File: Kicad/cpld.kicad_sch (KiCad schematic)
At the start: 16 parts, among them J2 Conn_01x06_Pin, U7 AMS1117-3.3, U9 XC95144XL-TQ144

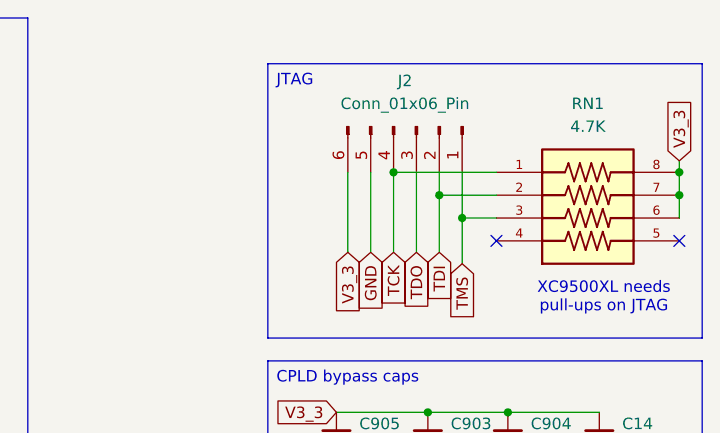
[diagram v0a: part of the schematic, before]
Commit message: Add more LCSC parts and mark some parts DNP
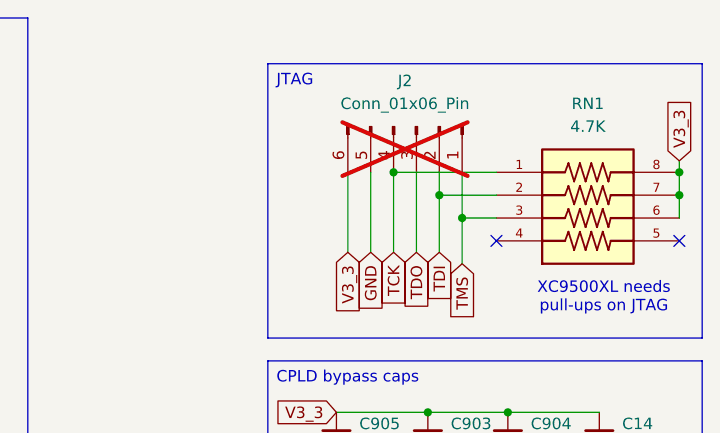
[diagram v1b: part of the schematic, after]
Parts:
- C14, C901, C902, C903, C904, C905, C906: LCSC Part # (none) -> C14663
- J2: LCSC Part # (none) -> C6332199; now not fitted
- RN1: footprint YC324-FK-071KL:RESCAXS127P508X320X70-8N -> CAY16_102J4LF:BO_CAY16; LCSC Part # (none) -> C327044
- U7: LCSC Part # (none) -> C6186
- U9: LCSC Part # (none) -> C1521137
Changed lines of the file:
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@@
 		(in_bom yes)
 		(on_board yes)
-		(dnp no)
+		(dnp yes)
 		(fields_autoplaced yes)
 		(property "Reference" "J2"
@@
 		(property "Description" "Generic connector, single row, 01x06, script generated"
 			(at 166.37 25.4 0)
+			(effects
+				(font
+					(size 1.27 1.27)
+				)
+				(hide yes)
+			)
+		)
+		(property "LCSC Part #" "C6332199"
+			(at 166.37 25.4 90)
 			(effects
 				(font
@@
 			)
 		)
+		(property "LCSC Part #" "C14663"
+			(at 157.48 68.58 0)
+			(effects
+				(font
+					(size 1.27 1.27)
+				)
+				(hide yes)
+			)
+		)
 		(pin "1"
 		)
@@
 			)
 		)
+		(property "LCSC Part #" "C1521137"
+			(at 67.31 104.14 0)
+			(effects
+				(font
+					(size 1.27 1.27)
+				)
+				(hide yes)
+			)
+		)
 		(pin "17"
 		)
@@
 			)
 		)
+		(property "LCSC Part #" ""
+			(at 160.02 97.79 0)
+			(effects
+				(font
+					(size 1.27 1.27)
+				)
+				(hide yes)
+			)
+		)
 		(pin "1"
 		)
@@
 			)
 		)
+		(property "LCSC Part #" "C14663"
+			(at 177.8 68.58 0)
+			(effects
+				(font
+					(size 1.27 1.27)
+				)
+				(hide yes)
+			)
+		)
 		(pin "1"
 		)
@@
 			)
 		)
+		(property "LCSC Part #" "C14663"
+			(at 176.53 59.69 0)
+			(effects
+				(font
+					(size 1.27 1.27)
+				)
+				(hide yes)
+			)
+		)
 		(pin "1"
 		)
@@
 		(property "Description" "Ferrite bead, small symbol"
 			(at 111.76 68.58 0)
+			(effects
+				(font
+					(size 1.27 1.27)
+				)
+				(hide yes)
+			)
+		)
+		(property "LCSC Part #" ""
+			(at 111.76 68.58 90)
 			(effects
 				(font
@@
 			)
 		)
+		(property "LCSC Part #" "C14663"
+			(at 157.48 59.69 0)
+			(effects
+				(font
+					(size 1.27 1.27)
+				)
+				(hide yes)
+			)
+		)
 		(pin "1"
 		)
@@
 			)
 		)
+		(property "LCSC Part #" "C14663"
+			(at 186.69 59.69 0)
+			(effects
+				(font
+					(size 1.27 1.27)
+				)
+				(hide yes)
+			)
+		)
 		(pin "2"
 		)
@@
 			)
 		)
+		(property "LCSC Part #" ""
+			(at 184.15 97.79 0)
+			(effects
+				(font
+					(size 1.27 1.27)
+				)
+				(hide yes)
+			)
+		)
 		(pin "1"
 		)
@@
 			)
 		)
+		(property "LCSC Part #" ""
+			(at 111.76 154.94 90)
+			(effects
+				(font
+					(size 1.27 1.27)
+				)
+				(hide yes)
+			)
+		)
 		(pin "1"
 		)
@@
 		(property "Description" "Ferrite bead, small symbol"
 			(at 111.76 144.78 0)
+			(effects
+				(font
+					(size 1.27 1.27)
+				)
+				(hide yes)
+			)
+		)
+		(property "LCSC Part #" ""
+			(at 111.76 144.78 90)
 			(effects
 				(font
@@
 			)
 		)
+		(property "LCSC Part #" "C14663"
+			(at 167.64 59.69 0)
+			(effects
+				(font
+					(size 1.27 1.27)
+				)
+				(hide yes)
+			)
+		)
 		(pin "2"
 		)
@@
 			)
 		)
+		(property "LCSC Part #" "C6186"
+			(at 173.99 92.71 0)
+			(effects
+				(font
+					(size 1.27 1.27)
+				)
+				(hide yes)
+			)
+		)
 		(pin "3"
 		)
@@
 			)
 		)
-		(property "Footprint" "YC324-FK-071KL:RESCAXS127P508X320X70-8N"
+		(property "Footprint" "CAY16_102J4LF:BO_CAY16"
 			(at 185.42 35.56 0)
 			(effects
@@
 				)
 				(justify bottom)
+				(hide yes)
+			)
+		)
+		(property "LCSC Part #" "C327044"
+			(at 185.42 35.56 0)
+			(effects
+				(font
+					(size 1.27 1.27)
+				)
 				(hide yes)
 			)
@@
 			(at 167.64 68.58 0)
 			(effects
+				(font
+					(size 1.27 1.27)
+				)
+				(hide yes)
+			)
+		)
+		(property "LCSC Part #" "C14663"
+			(at 167.64 68.58 0)
+			(effects

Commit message: Add remaining part numbers, remove C20, C30, C31
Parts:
- C701: LCSC Part # (none) -> C7194
- C702: LCSC Part # (none) -> C696813
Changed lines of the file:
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@@
 			)
 		)
-		(property "LCSC Part #" ""
+		(property "LCSC Part #" "C7194"
 			(at 160.02 97.79 0)
 			(effects
@@
 			)
 		)
-		(property "LCSC Part #" ""
+		(property "LCSC Part #" "C696813"
 			(at 184.15 97.79 0)
 			(effects

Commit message: Fix LCSC parts issues
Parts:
- FB6, FB7, FB8: LCSC Part # (none) -> C95177
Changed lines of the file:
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@@
 			)
 		)
-		(property "LCSC Part #" ""
+		(property "LCSC Part #" "C95177"
 			(at 111.76 68.58 90)
 			(effects
@@
 			)
 		)
-		(property "LCSC Part #" ""
+		(property "LCSC Part #" "C95177"
 			(at 111.76 154.94 90)
 			(effects
@@
 			)
 		)
-		(property "LCSC Part #" ""
+		(property "LCSC Part #" "C95177"
 			(at 111.76 144.78 90)
 			(effects

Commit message: Clean up schematics
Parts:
- removed C14: 100nF, Capacitor_SMD:C_0603_1608Metric_Pad1.08x0.95mm_HandSolder, symbol Device:C_Small
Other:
- moved on the sheet: C701, C702, C901, C902, C903, C904, C905, C906, U7

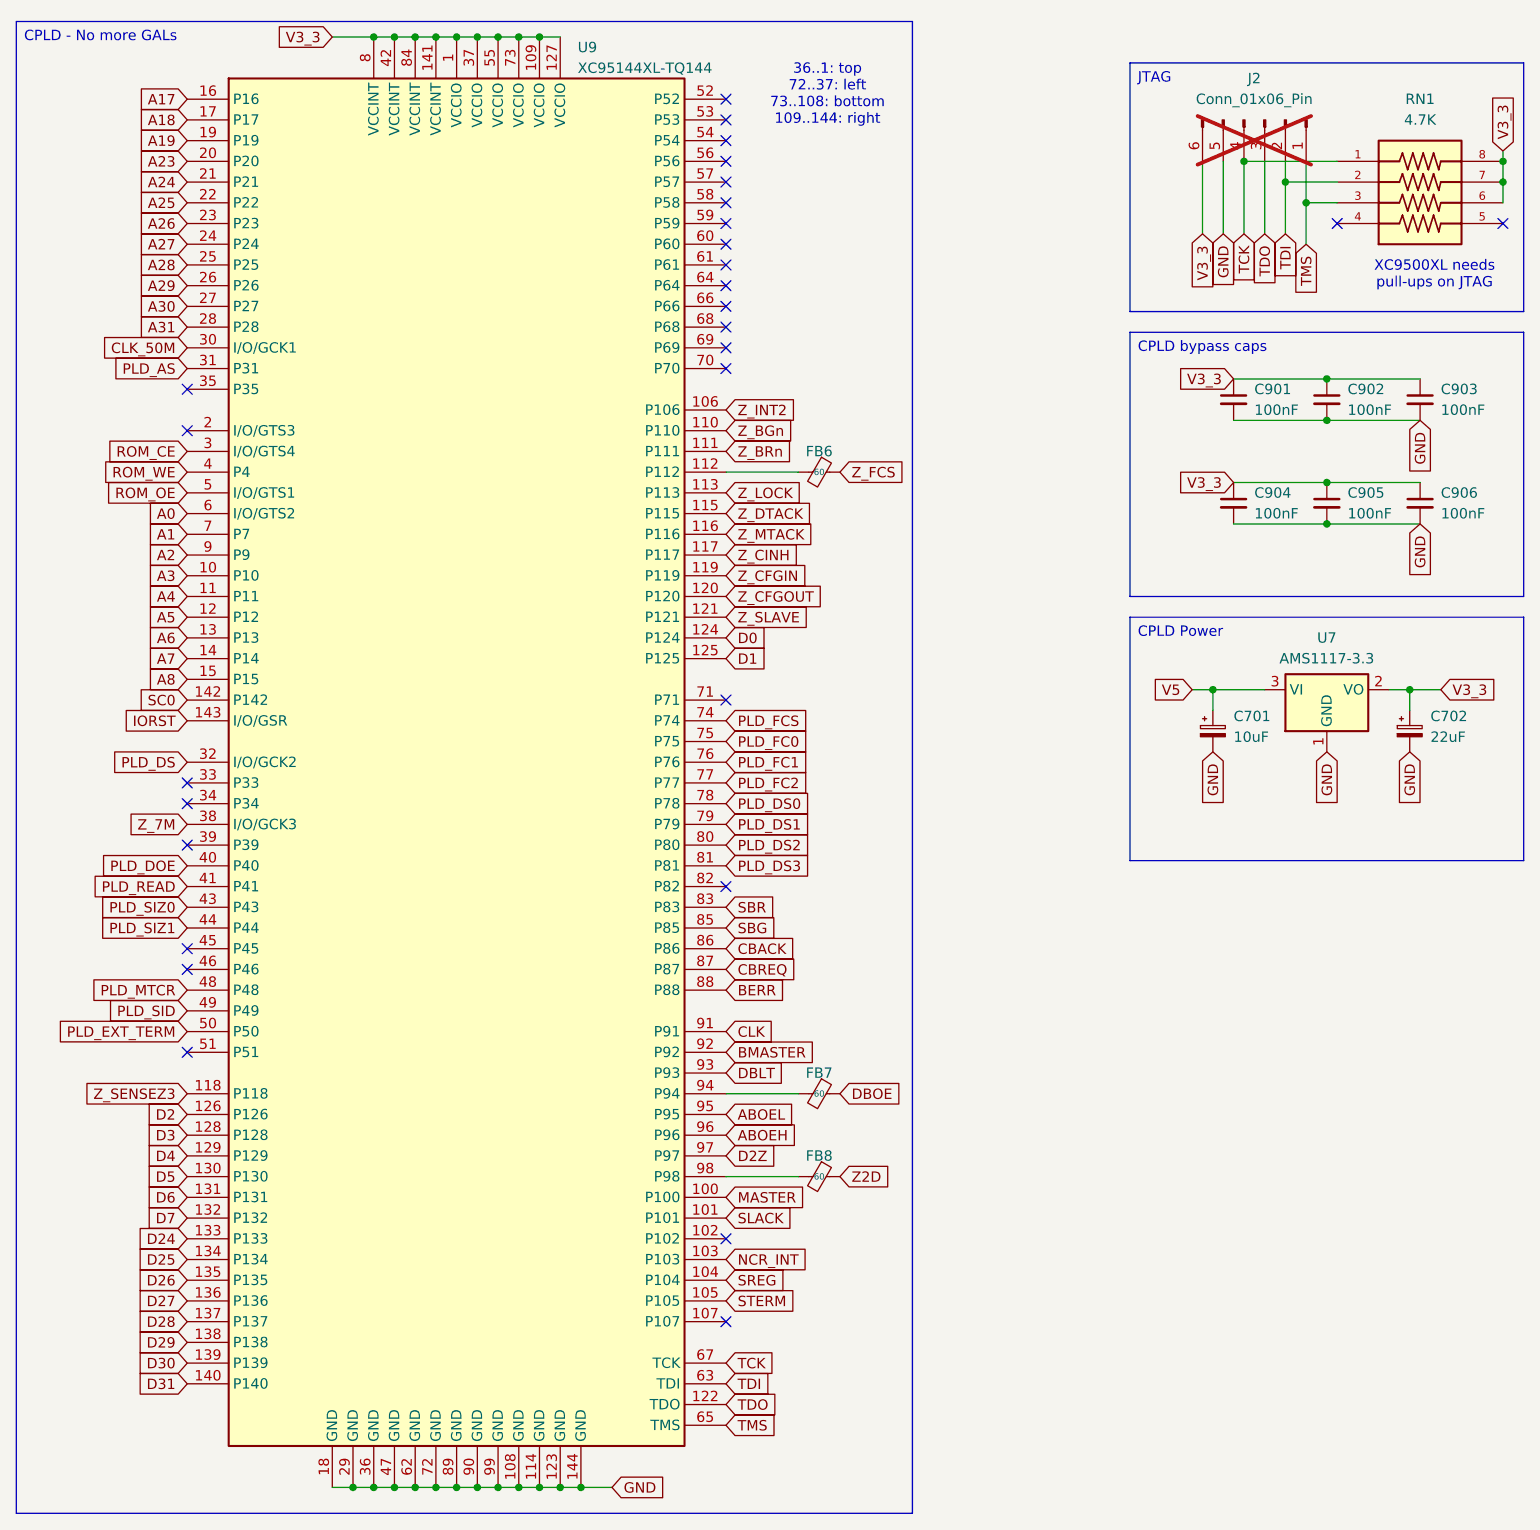
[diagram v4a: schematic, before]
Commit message: Add fiducials and clean up schematics
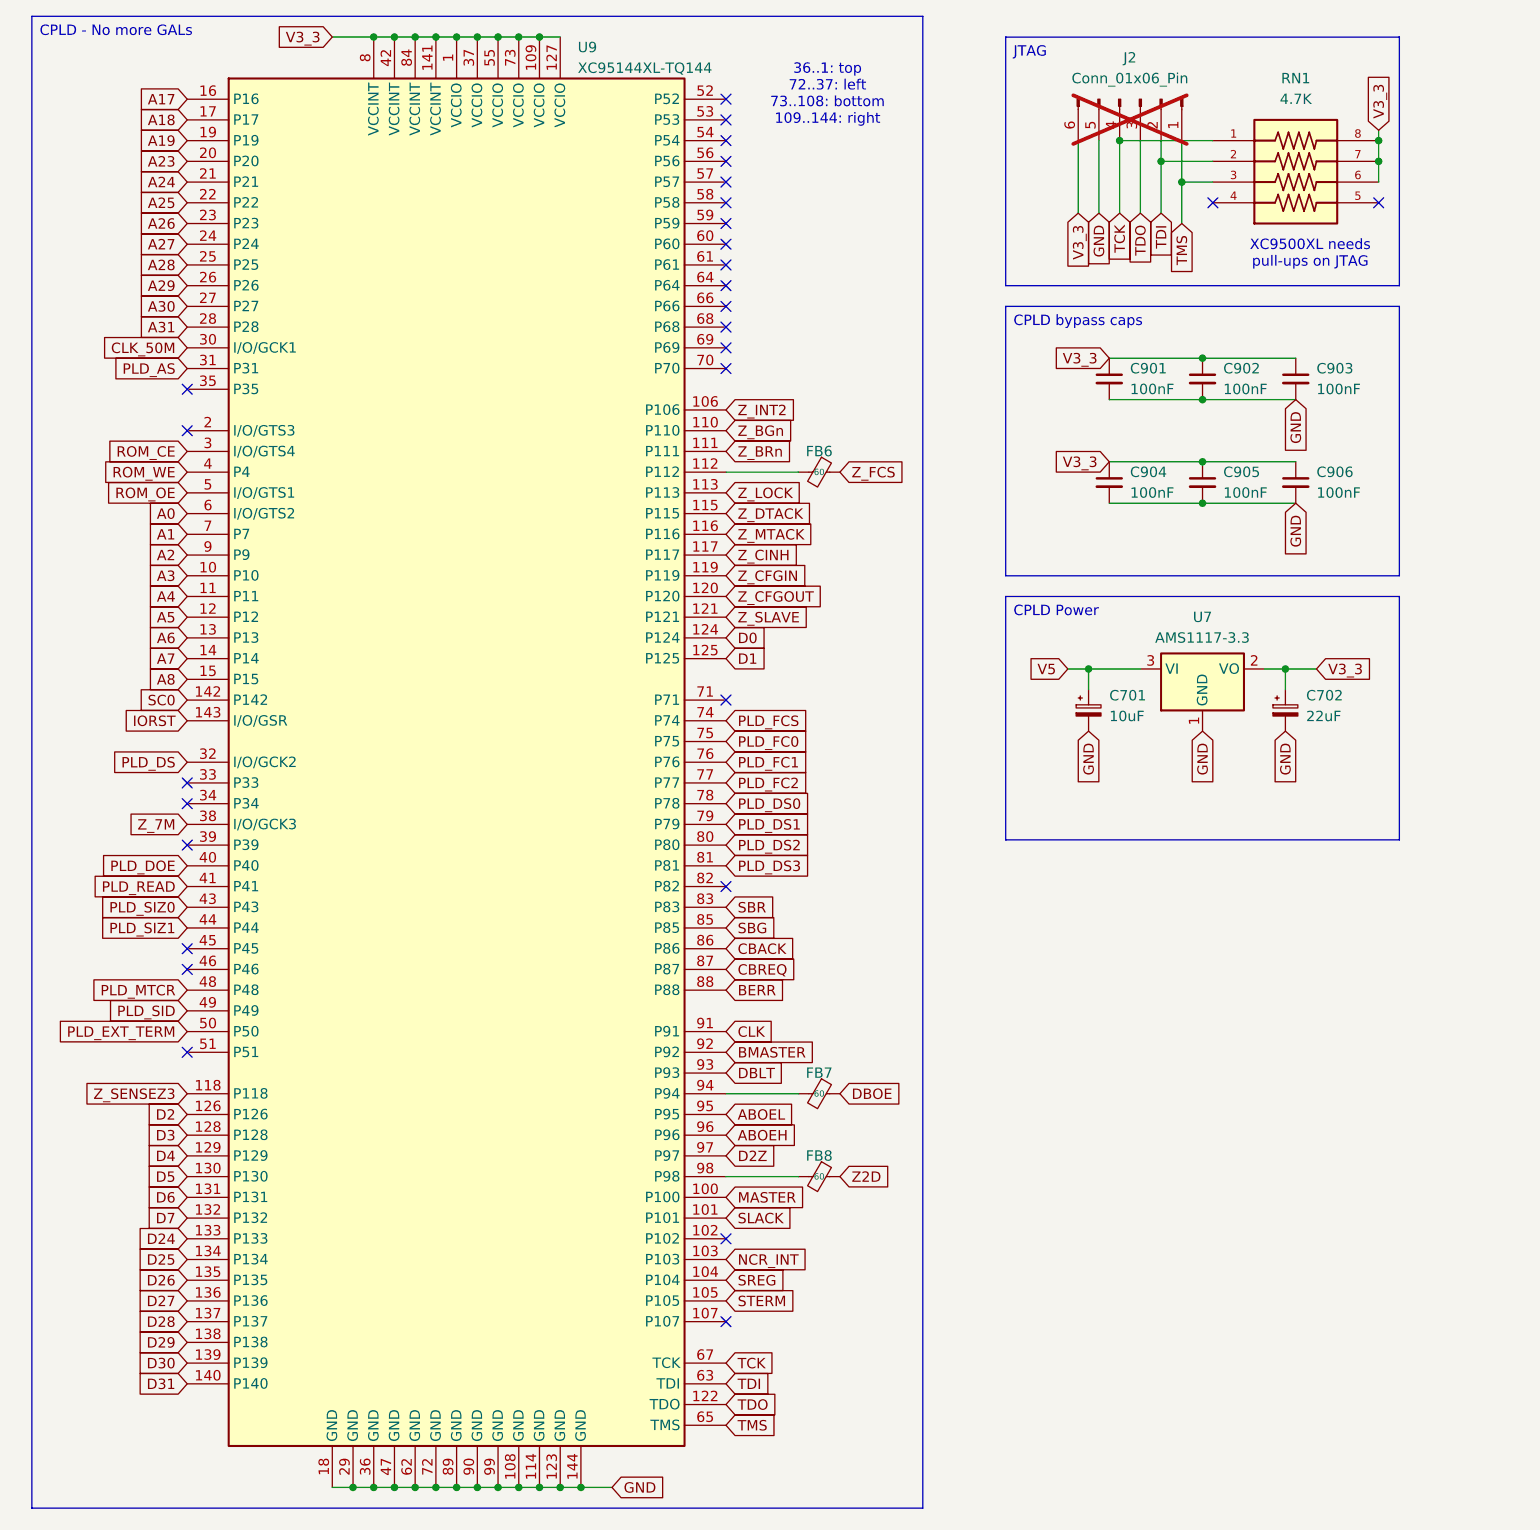
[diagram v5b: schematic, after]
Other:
- moved on the sheet: C701, C702, C901, C902, C903, C904, C905, C906, J2, RN1, U7

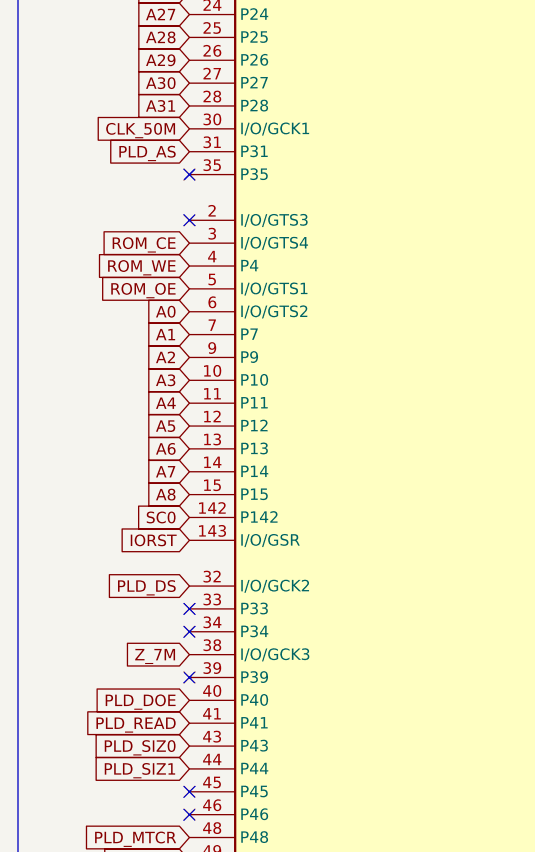
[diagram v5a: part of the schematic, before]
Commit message: Add SPI flash option and move flash to its own page
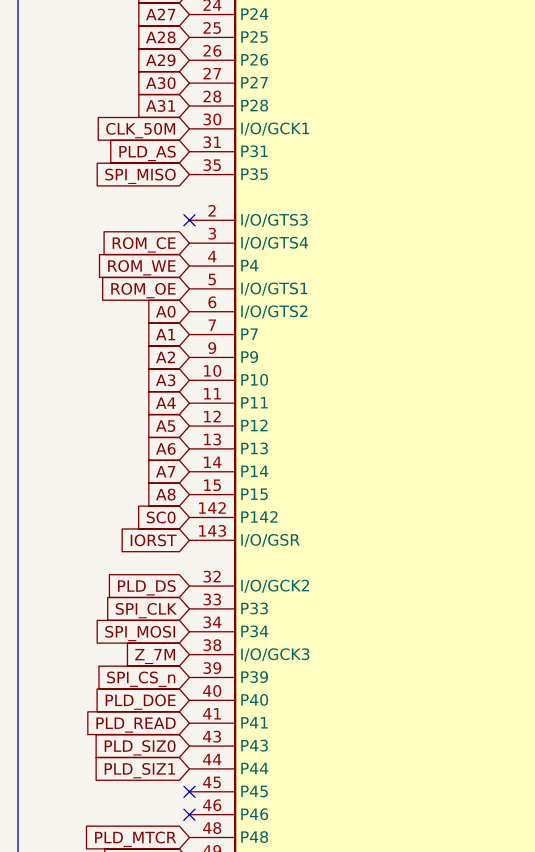
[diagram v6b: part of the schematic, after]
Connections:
- net SPI_CLK: now reaches U9.33 (P33)
- net SPI_MOSI: now reaches U9.34 (P34)
- net SPI_MISO: now reaches U9.35 (P35)
- net SPI_CS_n: now reaches U9.39 (P39)
- no-connect marks 28 -> 24
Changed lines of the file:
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@@
-	)
-	(no_connect
-		(at 34.29 109.22)
 	)
 	(no_connect
@@
 	)
 	(no_connect
-		(at 34.29 114.3)
-	)
-	(no_connect
 		(at 100.33 25.4)
 	)
@@
 	)
 	(no_connect
-		(at 34.29 106.68)
-	)
-	(no_connect
 		(at 100.33 30.48)
 	)
@@
 	)
 	(no_connect
-		(at 34.29 58.42)
-	)
-	(no_connect
 		(at 100.33 33.02)
 	)
@@
 		)
 	)
+	(global_label "SPI_MOSI"
+		(shape input)
+		(at 34.29 109.22 180)
+		(fields_autoplaced yes)
+		(effects
+			(font
+				(size 1.27 1.27)
+			)
+			(justify right)
+		)
+		(property "Intersheetrefs" "${INTERSHEET_REFS}"
+			(at 22.6567 109.22 0)
+			(effects
+				(font
+					(size 1.27 1.27)
+				)
+				(justify right)
+				(hide yes)
+			)
+		)
+	)
 	(global_label "A3"
 		(shape input)
@@
 		)
 	)
+	(global_label "SPI_CS_n"
+		(shape input)
+		(at 34.29 114.3 180)
+		(fields_autoplaced yes)
+		(effects
+			(font
+				(size 1.27 1.27)
+			)
+			(justify right)
+		)
+		(property "Intersheetrefs" "${INTERSHEET_REFS}"
+			(at 22.6568 114.3 0)
+			(effects
+				(font
+					(size 1.27 1.27)
+				)
+				(justify right)
+				(hide yes)
+			)
+		)
+	)
 	(global_label "Z_DTACK"
 		(shape input)
@@
 		)
 	)
+	(global_label "SPI_CLK"
+		(shape input)
+		(at 34.29 106.68 180)
+		(fields_autoplaced yes)
+		(effects
+			(font
+				(size 1.27 1.27)
+			)
+			(justify right)
+		)
+		(property "Intersheetrefs" "${INTERSHEET_REFS}"
+			(at 23.6848 106.68 0)
+			(effects
+				(font
+					(size 1.27 1.27)
+				)
+				(justify right)
+				(hide yes)
+			)
+		)
+	)
 	(global_label "D5"
 		(shape input)
@@
 			(effects
 				(font
+					(size 1.27 1.27)
+				)
+				(justify right)
+				(hide yes)
+			)
+		)
+	)
+	(global_label "SPI_MISO"
+		(shape input)
+		(at 34.29 58.42 180)
+		(fields_autoplaced yes)
+		(effects
+			(font
+				(size 1.27 1.27)
+			)
+			(justify right)
+		)
+		(property "Intersheetrefs" "${INTERSHEET_REFS}"
+			(at 22.6567 58.42 0)
+			(effects
+				(font
